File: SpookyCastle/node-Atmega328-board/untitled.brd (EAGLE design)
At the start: 63 x 40.5 mm, 20 parts, among them IC2 MEGA48/88/168-AU, J1 RJ11-6PTH

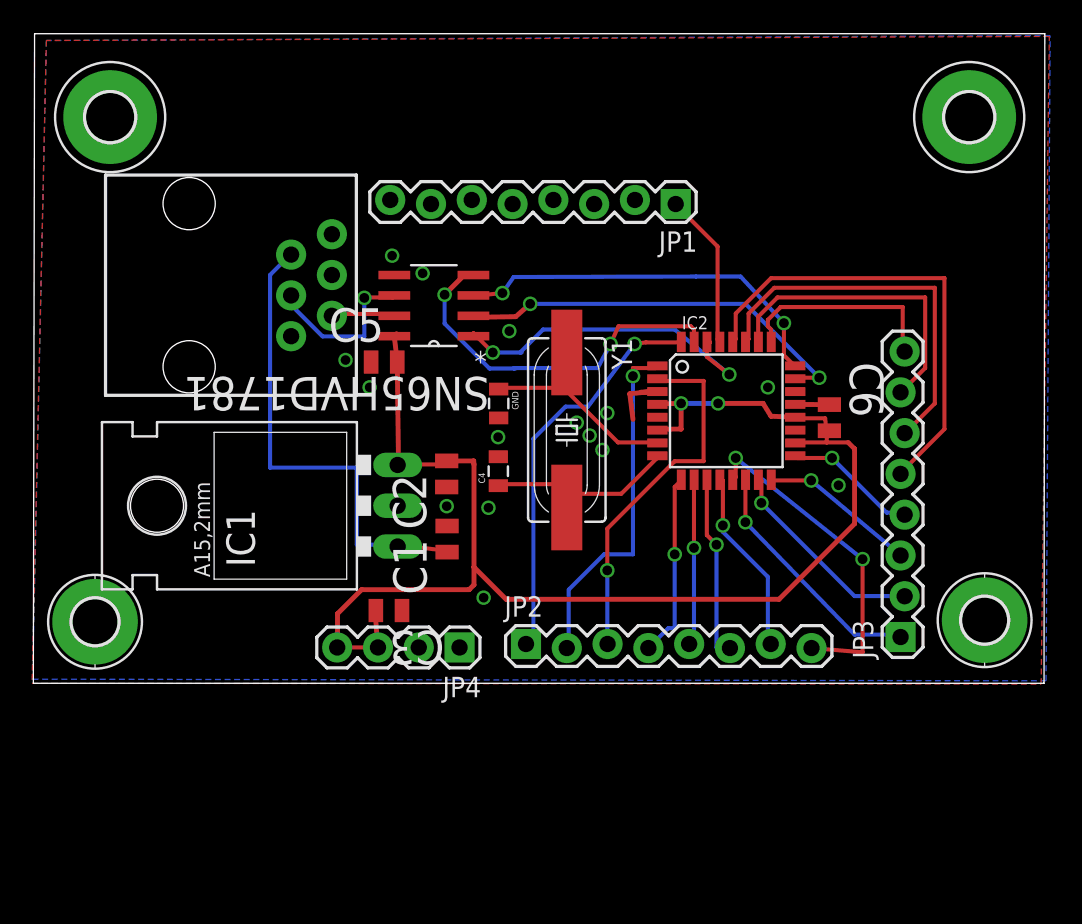
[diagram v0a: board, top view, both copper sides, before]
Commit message: Almost finished with the SpookyCastle atmega board, core protocol version 0.7.6: Pin ordering changed for rs485, updated PDF.
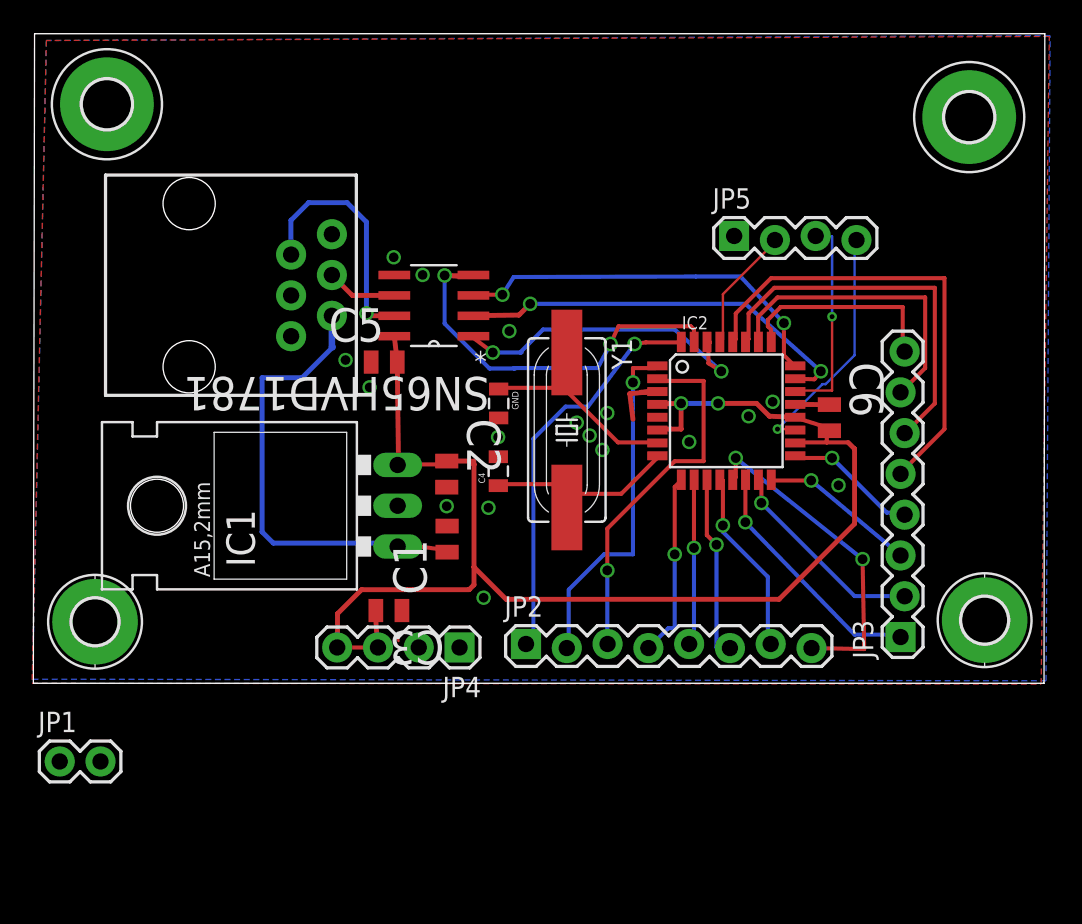
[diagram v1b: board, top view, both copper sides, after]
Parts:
- added JP5: (no value), SparkFun - Copy:1X04_LOCK
- JP1: device SparkFun - Copy:1X08_LOCK -> SparkFun - Copy:1X02
- moved JP1 51.8 mm to (2.10, 31.3), turned to 0 degrees
- moved H1 0.82 mm to (5.04, 72.2)
- turned C2 to 270 degrees
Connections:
- removed net N$1: J1.4, SN65HVD1781.6
- removed net N$2: J1.5, SN65HVD1781.7
- removed net N$3: C1.1, IC1.IN, J1.2
- new net A: J1.3, SN65HVD1781.6
- new net B: J1.2, SN65HVD1781.7
- new net VEXTERN: C1.1, IC1.IN, J1.5
- net GND: now also C2.2, J1.4, JP5.1; no longer C2.1, J1.3
- net N$22: now also JP5.2; no longer JP1.1
- net P19: now also JP5.4
- net P22: now also JP5.3
- net VCC: now also C2.1; no longer C2.2
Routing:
- net N$3: track 30.4 -> 0.00 mm
- net VEXTERN: track 0.00 -> 29.9 mm
- net B: track 0.00 -> 15.3 mm, vias 0 -> 1
- net P19: track 0.00 -> 15.0 mm, vias 0 -> 1
- net P22: track 0.00 -> 12.9 mm, vias 0 -> 1
- net N$1: track 10.5 -> 0.00 mm, vias 1 -> 0
- net A: track 0.00 -> 4.41 mm
- net N$2: track 4.05 -> 0.00 mm
- net N$22: track 10.9 -> 7.76 mm
- net RO: track 21.3 -> 20.1 mm
- net VCC: track 88.6 -> 88.0 mm
- net GND: track 5.96 -> 6.54 mm, vias 15 -> 17

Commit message: Almost done making SpookyCastle board fit in 5cmx5cm
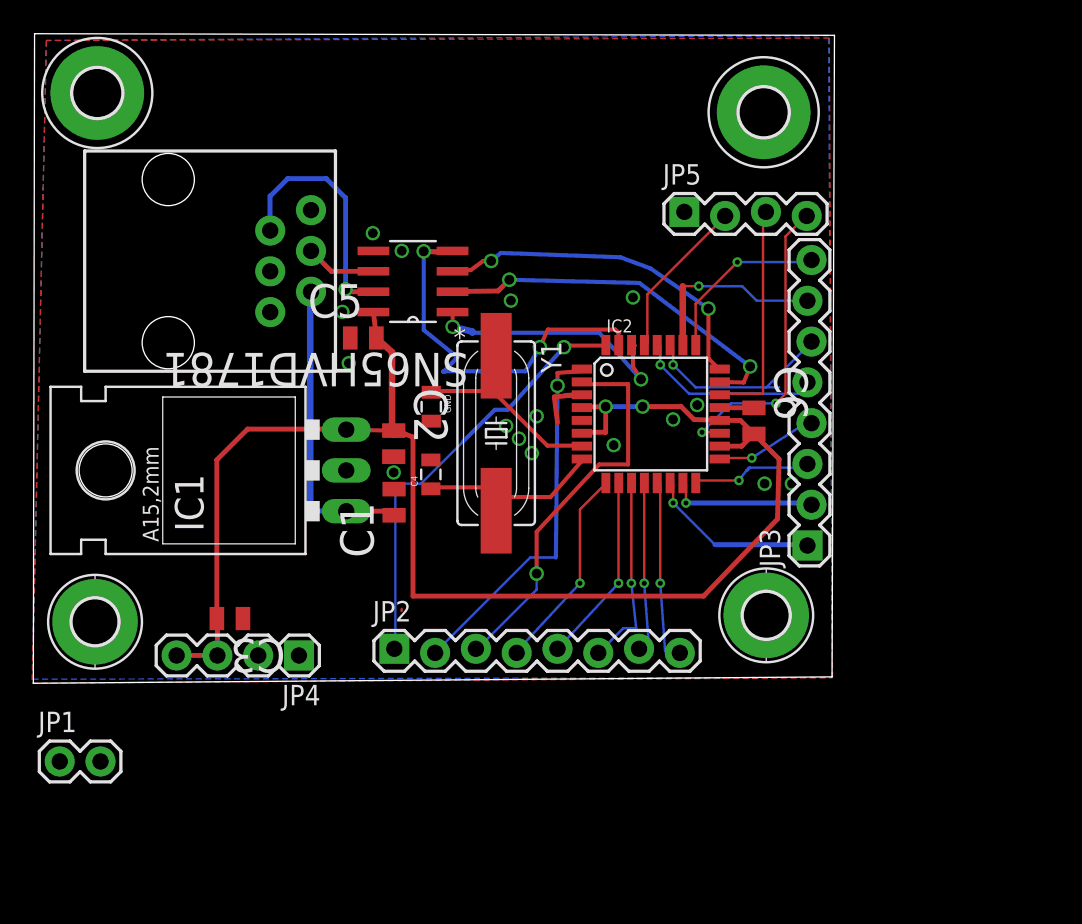
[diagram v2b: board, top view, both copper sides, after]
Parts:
- moved H4 13.6 mm to (46.1, 40.4)
- moved H2 12.8 mm to (45.9, 71.7)
- moved JP4 10.0 mm to (17.0, 37.9)
- moved C3 9.91 mm to (12.7, 40.2)
- moved JP2 8.21 mm to (22.9, 38.2)
- moved JP3 8.13 mm to (48.8, 44.7)
- moved IC2 4.70 mm to (38.9, 52.9)
- moved C6 4.70 mm to (45.3, 52.5)
- moved Y1 4.40 mm to (29.3, 51.7)
- moved C4 4.20 mm to (25.2, 49.2)
- moved GND 4.20 mm to (25.2, 53.4)
- moved C1 4.02 mm to (22.9, 47.4)
- moved IC1 3.88 mm to (16.1, 49.4)
- moved C2 3.81 mm to (22.9, 51.1)
- moved JP5 3.44 mm to (41.0, 65.4)
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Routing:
- net P28: track 29.1 -> 12.2 mm, vias 0 -> 1
- net P27: track 24.0 -> 12.5 mm, vias 0 -> 1
- net VEXTERN: track 29.9 -> 19.0 mm
- net N$11: track 20.4 -> 11.6 mm, vias 2 -> 1
- net P26: track 19.0 -> 12.7 mm, vias 0 -> 1
- net VCC: track 88.0 -> 94.1 mm
- net P19: track 15.0 -> 19.0 mm, vias 1 -> 2
- net N$12: track 15.4 -> 11.7 mm
- net N$13: track 12.9 -> 9.26 mm
- net RO: track 20.1 -> 16.6 mm
- net DE: track 24.2 -> 21.3 mm
- net N$22: track 7.76 -> 10.1 mm
- net RE: track 25.5 -> 23.2 mm
- net N$4: track 25.2 -> 27.4 mm
- net P25: track 13.0 -> 11.0 mm, vias 0 -> 1
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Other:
- board size 63 x 40.5 mm -> 49.9 x 40.5 mm

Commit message: Added option for 1210 capacitor on input of vreg, mitered some noise critical routing.
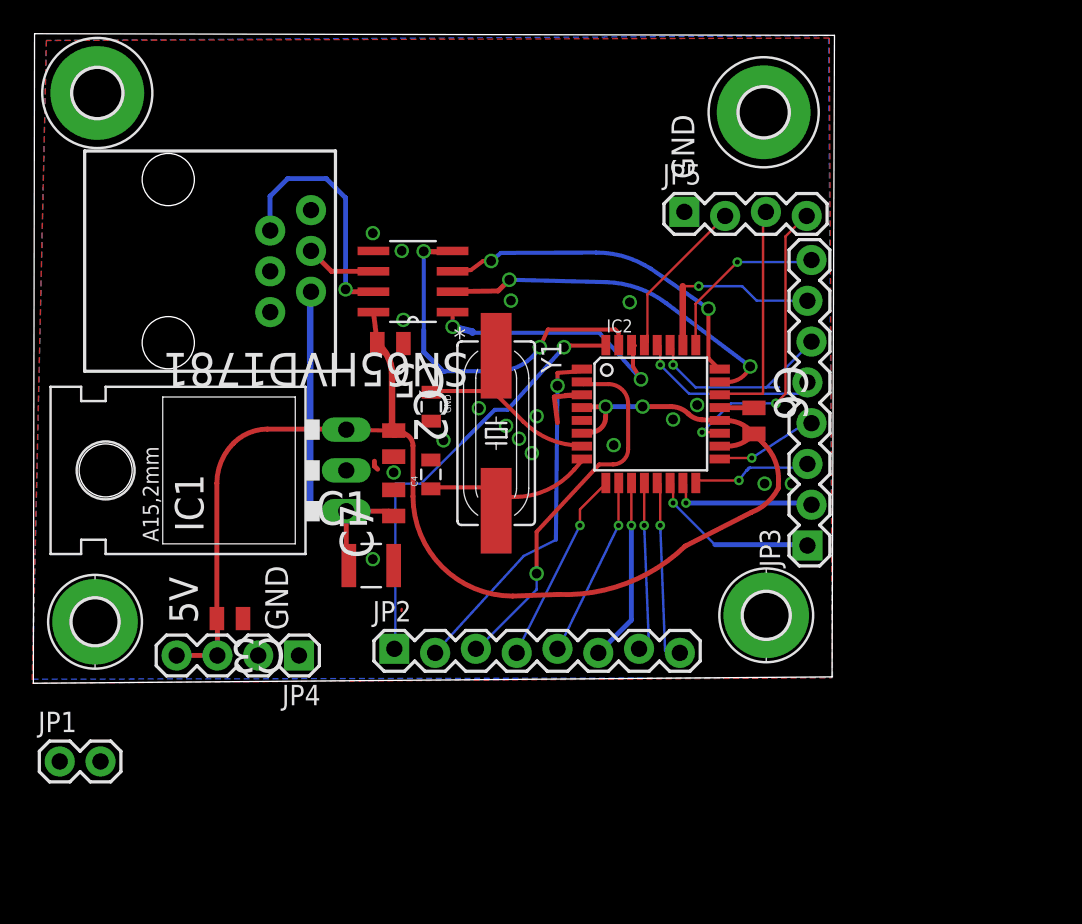
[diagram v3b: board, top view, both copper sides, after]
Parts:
- added C7: 1uF, Murata_By_element14_Batch_1:CAPC2013X135N
- C1: value 1uF -> 10uF; device Murata_By_element14_Batch_1:CAPC2013X135N -> Murata_By_element14_Batch_1:CAPC3225X270N
- moved C1 4.20 mm to (21.5, 43.5), turned to 0 degrees
- moved C5 1.72 mm to (22.7, 57.3), turned to 180 degrees
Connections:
- net GND: now also C7.2
- net VEXTERN: now also C7.1
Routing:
- net VCC: track 94.1 -> 86.1 mm
- net VEXTERN: track 19.0 -> 22.4 mm
- net DI: track 26.6 -> 25.3 mm
- net N$6: track 24.7 -> 23.5 mm
- net N$5: track 23.4 -> 22.7 mm
- net N$7: track 12.8 -> 12.2 mm
- net N$9: track 12.1 -> 11.4 mm
- net N$8: track 11.8 -> 11.2 mm
- net RE: track 23.2 -> 22.6 mm
- net N$1: track 0.00 -> 0.58 mm
- net GND: vias 16 -> 18
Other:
- board text added: "5V"
- board text added: "GND"

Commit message: Added option for bigger capacitor.
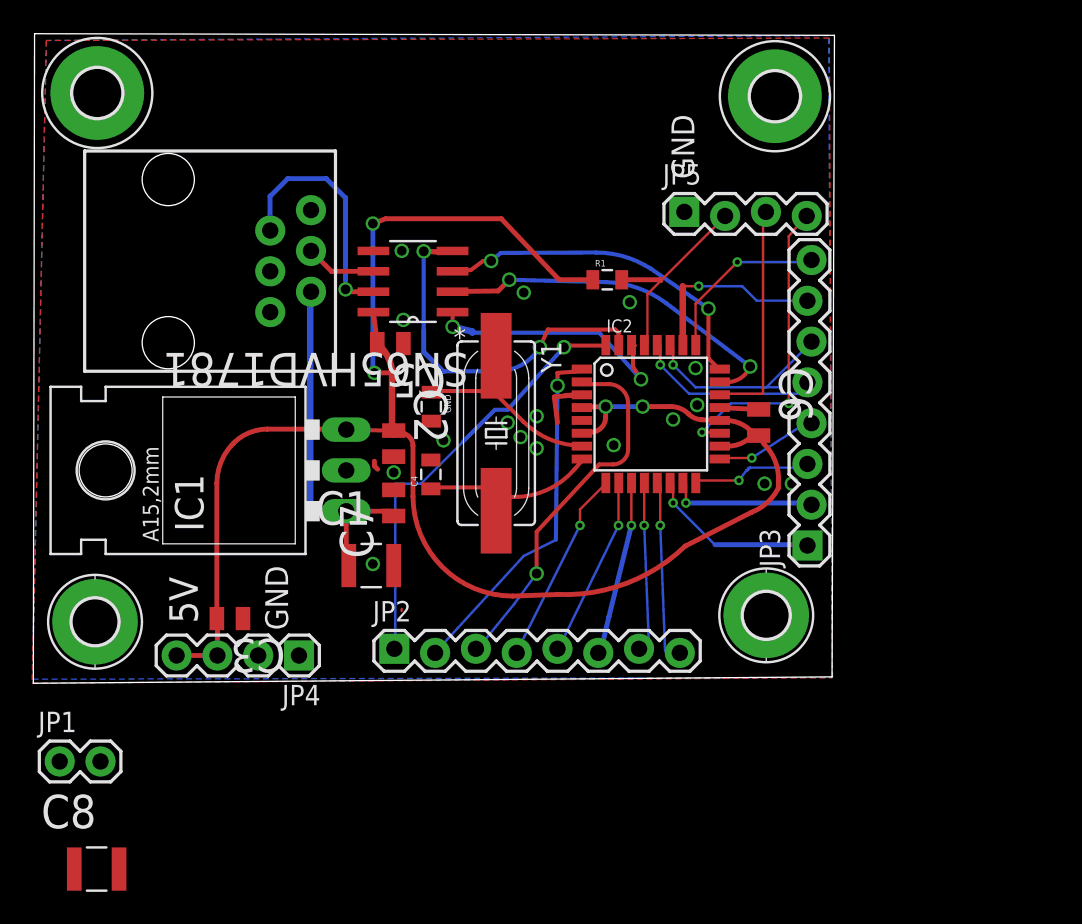
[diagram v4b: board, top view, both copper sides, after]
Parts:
- added C8: 10uF, Murata_By_element14_Batch_1:CAPC3225X270N
- added R1: 4.7k, SparkFun - Copy:0805
- moved H2 1.22 mm to (46.6, 72.7)
- moved C6 0.32 mm to (45.6, 52.4)
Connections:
- net N$22: now also R1.2
- net VCC: now also R1.1
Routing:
- net VCC: track 86.1 -> 112.2 mm, vias 2 -> 4
- net N$22: track 10.1 -> 12.6 mm
- net N$9: track 11.4 -> 10.9 mm
- net GND: track 6.09 -> 6.39 mm, vias 18 -> 17
